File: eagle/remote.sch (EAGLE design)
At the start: 22 parts, among them IC1 7805TV, Q1 16 Mhz, U1 ATMEGA328P-PU

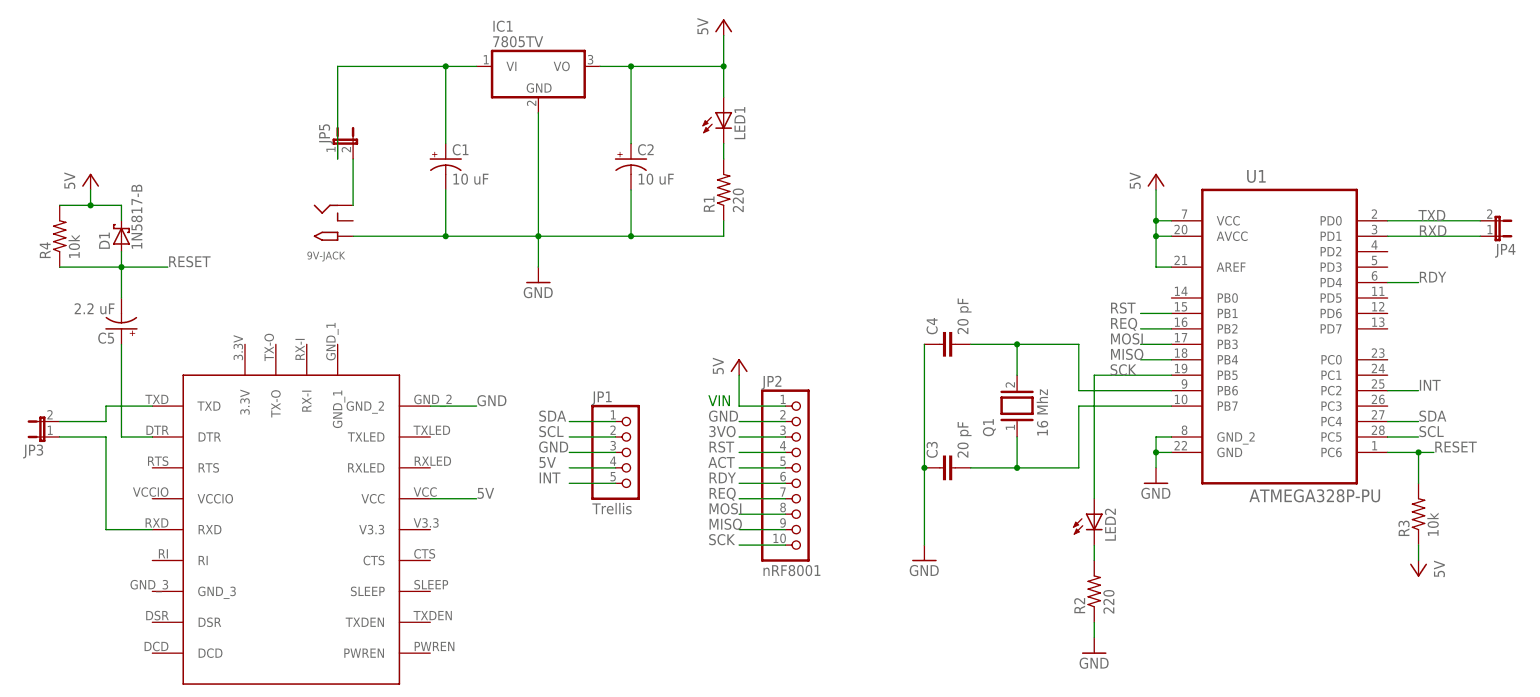
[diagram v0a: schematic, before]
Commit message: Reworked PCB so it is smaller.
Because I plan to order the PCB using www.oshpark.com, I used two layers
and tightened everything up.
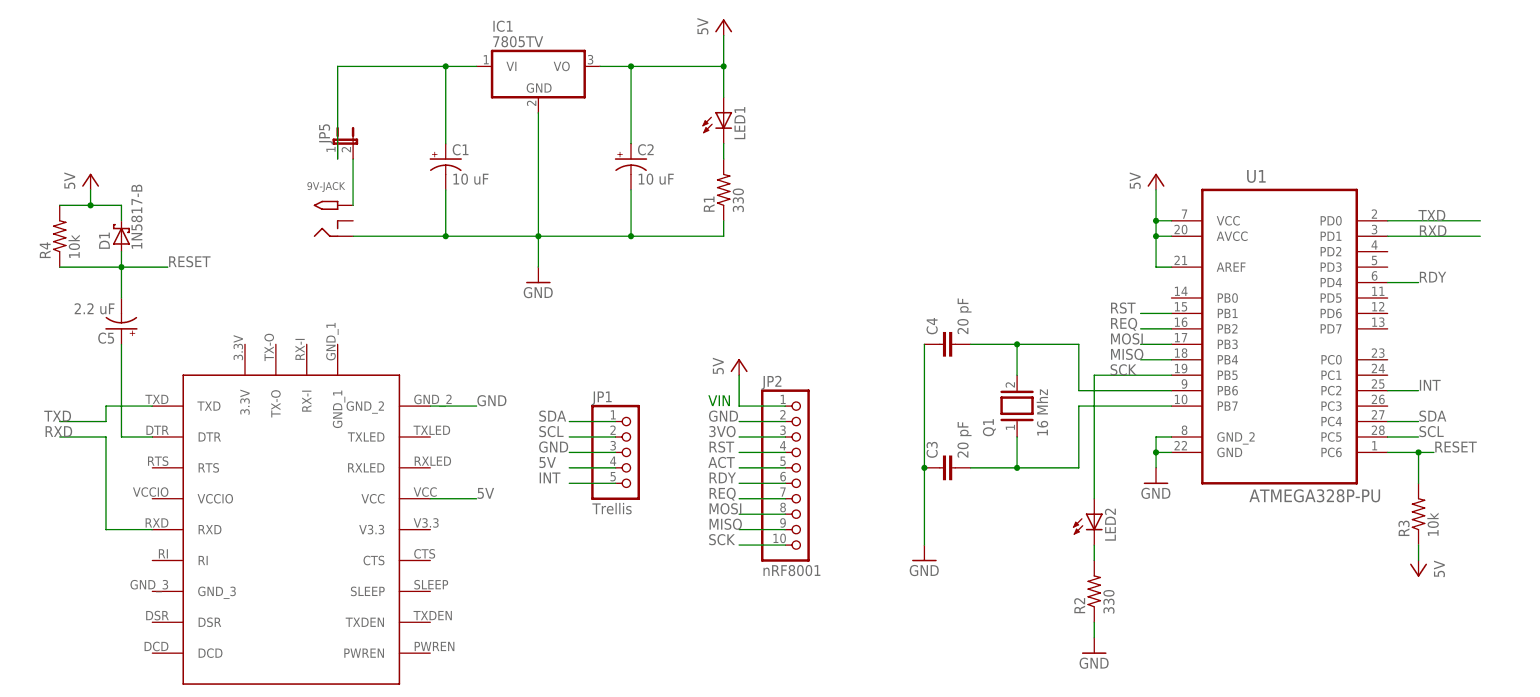
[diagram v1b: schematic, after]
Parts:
- removed JP3, JP4: (no value), jumper:JP1E
- LED1, LED2: device adafruit:LED5MM -> EE445L:LED3MM
- R1, R2: value 220 -> 330
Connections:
- removed net N$3: JP3.1, U$1.RXD
- removed net N$6: JP3.2, U$1.TXD
- net GND: now also 9V-JACK.RING; no longer 9V-JACK.TIP
- net N$8: now also 9V-JACK.TIP; no longer 9V-JACK.RING
- net RXD: now also U$1.RXD; no longer JP4.1
- net TXD: now also U$1.TXD; no longer JP4.2
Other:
- moved on the sheet: 9V-JACK
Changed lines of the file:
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@@
 <clearance class="0" value="0.254"/>
 </class>
-<class number="1" name="power" width="0.6096" drill="0">
-<clearance class="1" value="0.0254"/>
+<class number="1" name="power" width="0.7112" drill="0">
+<clearance class="1" value="0.254"/>
 </class>
 </classes>
@@
 <part name="C3" library="resistor" deviceset="C-EU" device="050-025X075" value="20 pF"/>
 <part name="C4" library="resistor" deviceset="C-EU" device="050-025X075" value="20 pF"/>
-<part name="LED1" library="adafruit" deviceset="LED" device="5MM"/>
-<part name="LED2" library="adafruit" deviceset="LED" device="5MM"/>
 <part name="Q1" library="special" deviceset="XTAL/S" device="" value="16 Mhz"/>
-<part name="R1" library="EE445L" deviceset="RESISTOR" device="0309/10" value="220"/>
-<part name="R2" library="EE445L" deviceset="RESISTOR" device="0309/10" value="220"/>
+<part name="R1" library="EE445L" deviceset="RESISTOR" device="0309/10" value="330"/>
+<part name="R2" library="EE445L" deviceset="RESISTOR" device="0309/10" value="330"/>
 <part name="9V-JACK" library="adafruit" deviceset="2.1MMJACK" device="THM" value="9V Input"/>
 <part name="GND2" library="supply1" deviceset="GND" device=""/>
@@
 <part name="P+4" library="supply1" deviceset="VCC" device="" value="5V"/>
 <part name="U$1" library="ft232" deviceset="FT232" device=""/>
-<part name="JP3" library="jumper" deviceset="JP1E" device=""/>
-<part name="JP4" library="jumper" deviceset="JP1E" device=""/>
 <part name="C5" library="resistor" deviceset="CPOL-US" device="B45181B" value="2.2 uF"/>
 <part name="P+5" library="supply1" deviceset="VCC" device="" value="5V"/>
@@
 <part name="D1" library="diode" deviceset="1N581*" device="" technology="7-B"/>
 <part name="JP5" library="jumper" deviceset="JP1E" device=""/>
+<part name="LED1" library="EE445L" deviceset="LED" device="3MM"/>
+<part name="LED2" library="EE445L" deviceset="LED" device="3MM"/>
 </parts>
 <sheets>
@@
 <instance part="C3" gate="G$1" x="76.2" y="22.86" rot="R90"/>
 <instance part="C4" gate="G$1" x="76.2" y="43.18" rot="R90"/>
-<instance part="LED1" gate="G$1" x="40.64" y="81.28"/>
-<instance part="LED2" gate="G$1" x="101.6" y="15.24"/>
 <instance part="Q1" gate="G$1" x="88.9" y="33.02" rot="R90"/>
 <instance part="R1" gate="G$1" x="40.64" y="68.58" rot="R90"/>
 <instance part="R2" gate="G$1" x="101.6" y="2.54" rot="R90"/>
-<instance part="9V-JACK" gate="G$1" x="-25.4" y="63.5" rot="MR180"/>
+<instance part="9V-JACK" gate="G$1" x="-25.4" y="63.5"/>
 <instance part="GND2" gate="1" x="10.16" y="53.34"/>
 <instance part="GND3" gate="1" x="73.66" y="7.62"/>
@@
 <instance part="P+4" gate="VCC" x="43.18" y="40.64"/>
 <instance part="U$1" gate="G$1" x="-30.48" y="15.24"/>
-<instance part="JP3" gate="A" x="-71.12" y="27.94" rot="R90"/>
-<instance part="JP4" gate="A" x="167.64" y="60.96" rot="MR90"/>
 <instance part="C5" gate="G$1" x="-58.42" y="45.72" rot="R180"/>
 <instance part="P+5" gate="VCC" x="-63.5" y="71.12"/>
@@
 <instance part="D1" gate="G$1" x="-58.42" y="60.96" rot="R90"/>
 <instance part="JP5" gate="A" x="-22.86" y="76.2"/>
+<instance part="LED1" gate="G$1" x="40.64" y="81.28"/>
+<instance part="LED2" gate="G$1" x="101.6" y="15.24"/>
 </instances>
 <busses>
@@
 <wire x1="25.4" y1="68.58" x2="25.4" y2="60.96" width="0.1524" layer="91"/>
 <junction x="25.4" y="60.96"/>
-<pinref part="9V-JACK" gate="G$1" pin="TIP"/>
+<pinref part="9V-JACK" gate="G$1" pin="RING"/>
 <wire x1="-20.32" y1="60.96" x2="-5.08" y2="60.96" width="0.1524" layer="91"/>
 <junction x="-5.08" y="60.96"/>
@@
 <segment>
 <pinref part="R1" gate="G$1" pin="2"/>
+<wire x1="40.64" y1="73.66" x2="40.64" y2="76.2" width="0.1524" layer="91"/>
 <pinref part="LED1" gate="G$1" pin="C"/>
-<wire x1="40.64" y1="73.66" x2="40.64" y2="76.2" width="0.1524" layer="91"/>
 </segment>
 </net>
@@
 <net name="N$9" class="0">
 <segment>
-<pinref part="LED2" gate="G$1" pin="C"/>
 <pinref part="R2" gate="G$1" pin="2"/>
 <wire x1="101.6" y1="10.16" x2="101.6" y2="7.62" width="0.1524" layer="91"/>
+<pinref part="LED2" gate="G$1" pin="C"/>
 </segment>
 </net>
@@
 <wire x1="114.3" y1="38.1" x2="101.6" y2="38.1" width="0.1524" layer="91"/>
 <wire x1="101.6" y1="38.1" x2="101.6" y2="17.78" width="0.1524" layer="91"/>
+<label x="104.14" y="38.1" size="1.778" layer="95"/>
 <pinref part="LED2" gate="G$1" pin="A"/>
-<label x="104.14" y="38.1" size="1.778" layer="95"/>
 </segment>
 </net>
@@
 <segment>
 <pinref part="P+1" gate="VCC" pin="VCC"/>
-<pinref part="LED1" gate="G$1" pin="A"/>
 <wire x1="40.64" y1="83.82" x2="40.64" y2="88.9" width="0.1524" layer="91"/>
 <pinref part="IC1" gate="A1" pin="VO"/>
@@
 <wire x1="25.4" y1="76.2" x2="25.4" y2="88.9" width="0.1524" layer="91"/>
 <junction x="25.4" y="88.9"/>
+<pinref part="LED1" gate="G$1" pin="A"/>
 </segment>
 <segment>
@@
 <pinref part="U1" gate="A" pin="PD0"/>
 <label x="154.94" y="63.5" size="1.778" layer="95"/>
-<pinref part="JP4" gate="A" pin="2"/>
 <wire x1="165.1" y1="63.5" x2="149.86" y2="63.5" width="0.1524" layer="91"/>
+</segment>
+<segment>
+<pinref part="U$1" gate="G$1" pin="TXD"/>
+<wire x1="-53.34" y1="33.02" x2="-60.96" y2="33.02" width="0.1524" layer="91"/>
+<wire x1="-60.96" y1="33.02" x2="-60.96" y2="30.48" width="0.1524" layer="91"/>
+<wire x1="-60.96" y1="30.48" x2="-68.58" y2="30.48" width="0.1524" layer="91"/>
+<label x="-71.12" y="30.48" size="1.778" layer="95"/>
 </segment>
 </net>
@@
 <pinref part="U1" gate="A" pin="PD1"/>
 <label x="154.94" y="60.96" size="1.778" layer="95"/>
-<pinref part="JP4" gate="A" pin="1"/>
 <wire x1="165.1" y1="60.96" x2="149.86" y2="60.96" width="0.1524" layer="91"/>
 </segment>
-</net>
-<net name="N$3" class="0">
 <segment>
 <pinref part="U$1" gate="G$1" pin="RXD"/>
 <wire x1="-53.34" y1="12.7" x2="-60.96" y2="12.7" width="0.1524" layer="91"/>
 <wire x1="-60.96" y1="12.7" x2="-60.96" y2="27.94" width="0.1524" layer="91"/>
-<pinref part="JP3" gate="A" pin="1"/>
 <wire x1="-60.96" y1="27.94" x2="-68.58" y2="27.94" width="0.1524" layer="91"/>
-</segment>
-</net>
-<net name="N$6" class="0">
-<segment>
-<pinref part="U$1" gate="G$1" pin="TXD"/>
-<wire x1="-53.34" y1="33.02" x2="-60.96" y2="33.02" width="0.1524" layer="91"/>
-<wire x1="-60.96" y1="33.02" x2="-60.96" y2="30.48" width="0.1524" layer="91"/>
-<pinref part="JP3" gate="A" pin="2"/>
-<wire x1="-60.96" y1="30.48" x2="-68.58" y2="30.48" width="0.1524" layer="91"/>
+<label x="-71.12" y="27.94" size="1.778" layer="95"/>
 </segment>
 </net>
@@
 </segment>
 </net>
-<net name="N$8" class="0">
-<segment>
-<pinref part="9V-JACK" gate="G$1" pin="RING"/>
-<wire x1="-20.32" y1="66.04" x2="-20.32" y2="73.66" width="0.1524" layer="91"/>
+<net name="N$8" class="1">
+<segment>
 <pinref part="JP5" gate="A" pin="2"/>
-</segment>
-</net>
+<pinref part="9V-JACK" gate="G$1" pin="TIP"/>
+<wire x1="-20.32" y1="73.66" x2="-20.32" y2="66.04" width="0.1524" layer="91"/>
+</segment>
+</net>
